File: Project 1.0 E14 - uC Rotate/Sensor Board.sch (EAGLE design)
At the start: 107 parts, among them IC1 LT1963EST-1.5, IC2 LT1963EST-1.5, IC4 LT1963EST-1.5, J1 501568-0207, J2 501568-0207, J3 SD-105027-101, U1 MAG3110, U10 ADXL362, U11 TM4C1233H6PM, U14 TXB0108, U15 ADT7301, U17 LSM9DS0, U19 MAX21000, U2 H3LIS331DLTR, U21 SN74HC42, U22 SI7013, U3 L3GD20H, U4 LPS331AP, U5 MPL3115A2, U6 LSM303D, U7 501568-0407, U8 STLM20, U9 LIS3DH

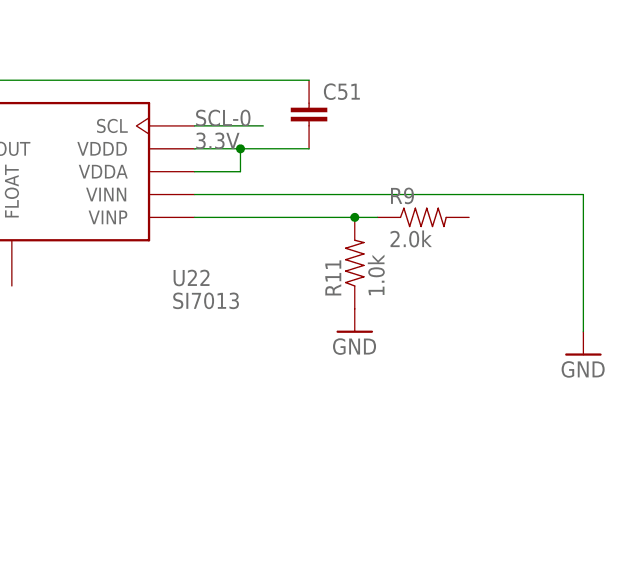
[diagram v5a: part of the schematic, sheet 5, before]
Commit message: Sensor Test Board: Resolved issue 22 by changing from LSG3 INT1 to INT2 allowing for an interupt to be genarated on a watermark event
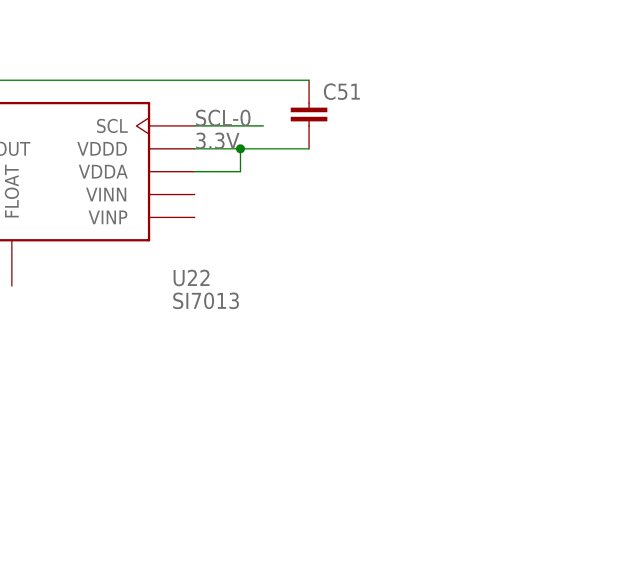
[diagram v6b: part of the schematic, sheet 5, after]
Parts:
- removed R11: 1.0k, Kas-Passives:RESISTOR
- removed R9: 2.0k, Kas-Passives:RESISTOR
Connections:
- removed net INT1-L3GD: U11.PC5, U3.INT1
- removed net N$2: R11.2, R9.1, U22.VINP
- new net INT2-L3GD: U11.PC5, U3.INT2
- net GND: no longer R11.1, U22.VINN
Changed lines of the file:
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@@
 <part name="R8" library="Kas-Passives" deviceset="RESISTOR" device="" value="0"/>
 <part name="U22" library="Kas-Sensors" deviceset="SI7013" device=""/>
-<part name="R9" library="Kas-Passives" deviceset="RESISTOR" device="" value="2.0k"/>
-<part name="R11" library="Kas-Passives" deviceset="RESISTOR" device="" value="1.0k"/>
 <part name="GND21" library="SparkFun-Aesthetics" deviceset="GND" device=""/>
 <part name="C51" library="Kas-Passives" deviceset="CAPACITOR" device="0402"/>
@@
 <part name="R14" library="Kas-Passives" deviceset="RESISTOR" device="" value="10k"/>
 <part name="GND22" library="SparkFun-Aesthetics" deviceset="GND" device=""/>
-<part name="GND39" library="SparkFun-Aesthetics" deviceset="GND" device=""/>
 <part name="GND40" library="SparkFun-Aesthetics" deviceset="GND" device=""/>
 <part name="GND41" library="SparkFun-Aesthetics" deviceset="GND" device=""/>
 <part name="GND45" library="SparkFun-Aesthetics" deviceset="GND" device=""/>
 <part name="GND46" library="SparkFun-Aesthetics" deviceset="GND" device=""/>
-<part name="GND49" library="SparkFun-Aesthetics" deviceset="GND" device=""/>
 <part name="J2" library="Kas-Connectors" deviceset="501568-0207" device=""/>
 <part name="LED5" library="eagle-ltspice" deviceset="LED_E" device="SML0603" value="Green"/>
@@
 <part name="GND50" library="SparkFun-Aesthetics" deviceset="GND" device=""/>
 <part name="GND51" library="SparkFun-Aesthetics" deviceset="GND" device=""/>
+<part name="GND52" library="SparkFun-Aesthetics" deviceset="GND" device=""/>
 </parts>
 <sheets>
@@
 </segment>
 </net>
-<net name="INT1-L3GD" class="0">
+<net name="INT2-L3GD" class="0">
 <segment>
 <pinref part="U11" gate="G$1" pin="PC5"/>
@@
 </segment>
 </net>
-<net name="INT1-L3GD" class="0">
-<segment>
-<pinref part="U3" gate="G$1" pin="INT1"/>
-<wire x1="43.18" y1="5.08" x2="43.18" y2="2.54" width="0.1524" layer="91"/>
+<net name="INT2-L3GD" class="0">
+<segment>
 <label x="25.4" y="2.54" size="1.778" layer="95"/>
-<wire x1="43.18" y1="2.54" x2="25.4" y2="2.54" width="0.1524" layer="91"/>
+<pinref part="U3" gate="G$1" pin="INT2"/>
+<wire x1="40.64" y1="2.54" x2="25.4" y2="2.54" width="0.1524" layer="91"/>
+<wire x1="40.64" y1="5.08" x2="40.64" y2="2.54" width="0.1524" layer="91"/>
 </segment>
 </net>
@@
 <instance part="GND44" gate="1" x="50.8" y="-17.78"/>
 <instance part="U22" gate="G$1" x="101.6" y="-7.62"/>
-<instance part="R9" gate="G$1" x="144.78" y="-12.7"/>
-<instance part="R11" gate="G$1" x="137.16" y="-17.78" rot="R90"/>
 <instance part="GND21" gate="1" x="73.66" y="-12.7"/>
 <instance part="C51" gate="G$1" x="132.08" y="-2.54"/>
-<instance part="GND39" gate="1" x="137.16" y="-25.4"/>
-<instance part="GND49" gate="1" x="162.56" y="-27.94"/>
 </instances>
 <busses>
@@
 <junction x="73.66" y="-10.16"/>
 <pinref part="C51" gate="G$1" pin="1"/>
-</segment>
-<segment>
-<pinref part="U22" gate="G$1" pin="VINN"/>
-<pinref part="GND49" gate="1" pin="GND"/>
-<wire x1="119.38" y1="-10.16" x2="162.56" y2="-10.16" width="0.1524" layer="91"/>
-<wire x1="162.56" y1="-10.16" x2="162.56" y2="-25.4" width="0.1524" layer="91"/>
-</segment>
-<segment>
-<pinref part="R11" gate="G$1" pin="1"/>
-<pinref part="GND39" gate="1" pin="GND"/>
 </segment>
 <segment>
@@
 </segment>
 </net>
-<net name="N$2" class="0">
-<segment>
-<pinref part="R9" gate="G$1" pin="1"/>
-<pinref part="R11" gate="G$1" pin="2"/>
-<wire x1="139.7" y1="-12.7" x2="137.16" y2="-12.7" width="0.1524" layer="91"/>
-<pinref part="U22" gate="G$1" pin="VINP"/>
-<wire x1="137.16" y1="-12.7" x2="119.38" y2="-12.7" width="0.1524" layer="91"/>
-<junction x="137.16" y="-12.7"/>
-</segment>
-</net>
 </nets>
 </sheet>
@@
 <instance part="GND50" gate="1" x="-25.4" y="2.54"/>
 <instance part="GND51" gate="1" x="27.94" y="2.54"/>
+<instance part="GND52" gate="1" x="30.48" y="-15.24"/>
 </instances>
 <busses>
@@
 <pinref part="U14" gate="G$1" pin="GND"/>
 <wire x1="15.24" y1="-12.7" x2="30.48" y2="-12.7" width="0.1524" layer="91"/>
-<label x="22.86" y="-12.7" size="1.778" layer="95"/>
-</segment>
-<segment>
+<pinref part="GND52" gate="1" pin="GND"/>
+</segment>
+<segment>

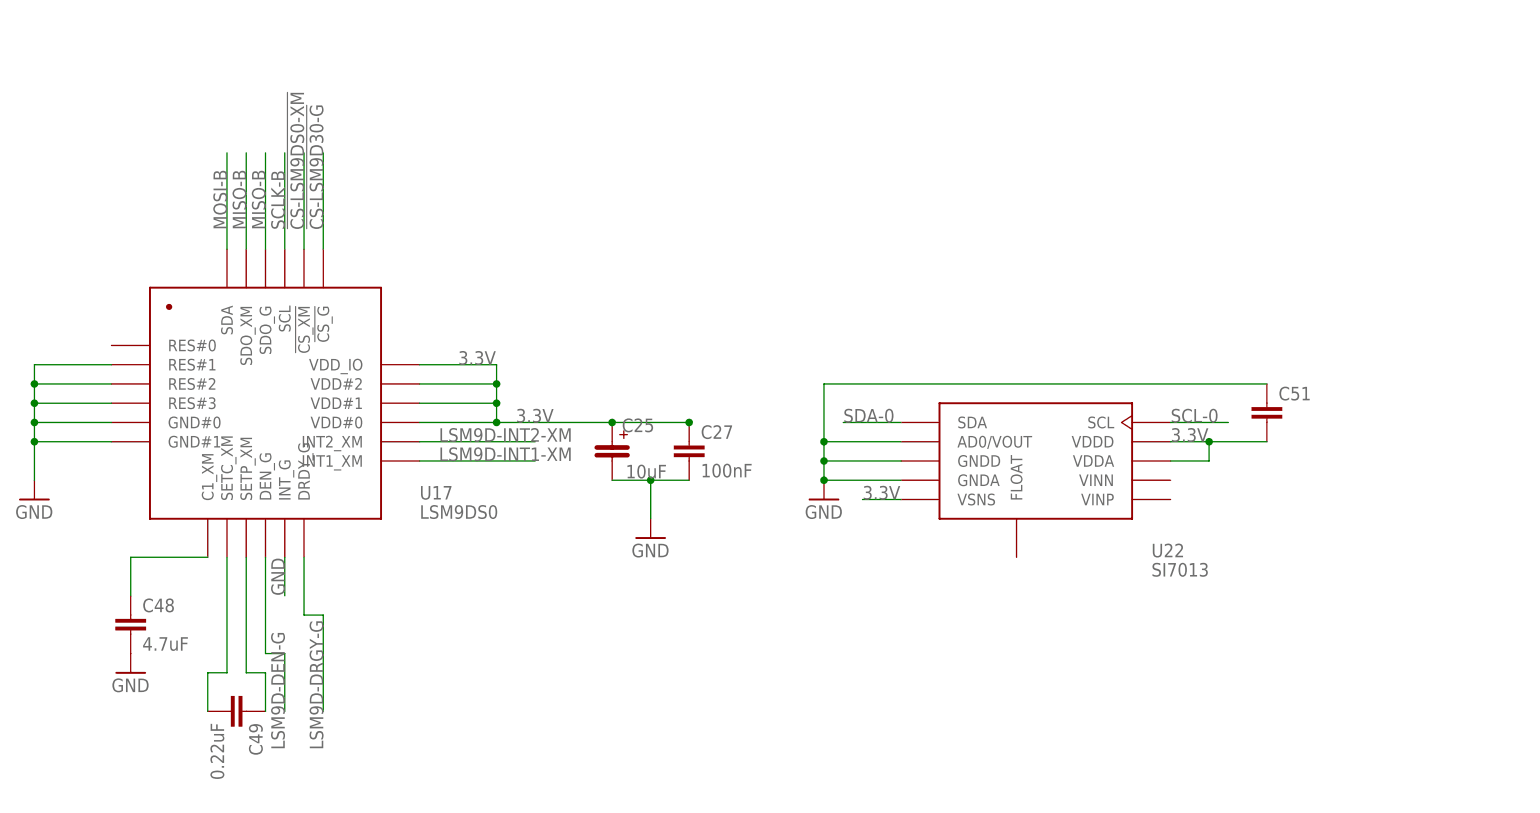
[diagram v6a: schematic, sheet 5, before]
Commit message: Sensor Test Board: Added power lines for all components. Split power into two groups A (130 mA) and B (177 mA). A has sensors connected except for the STLM20. B has the remaing components.  I2C test points were moved to allow for power routing to the right side sensors. Intterupt lines for ADXL362 and MPL3115A2 where swapped to allow for easier power routing
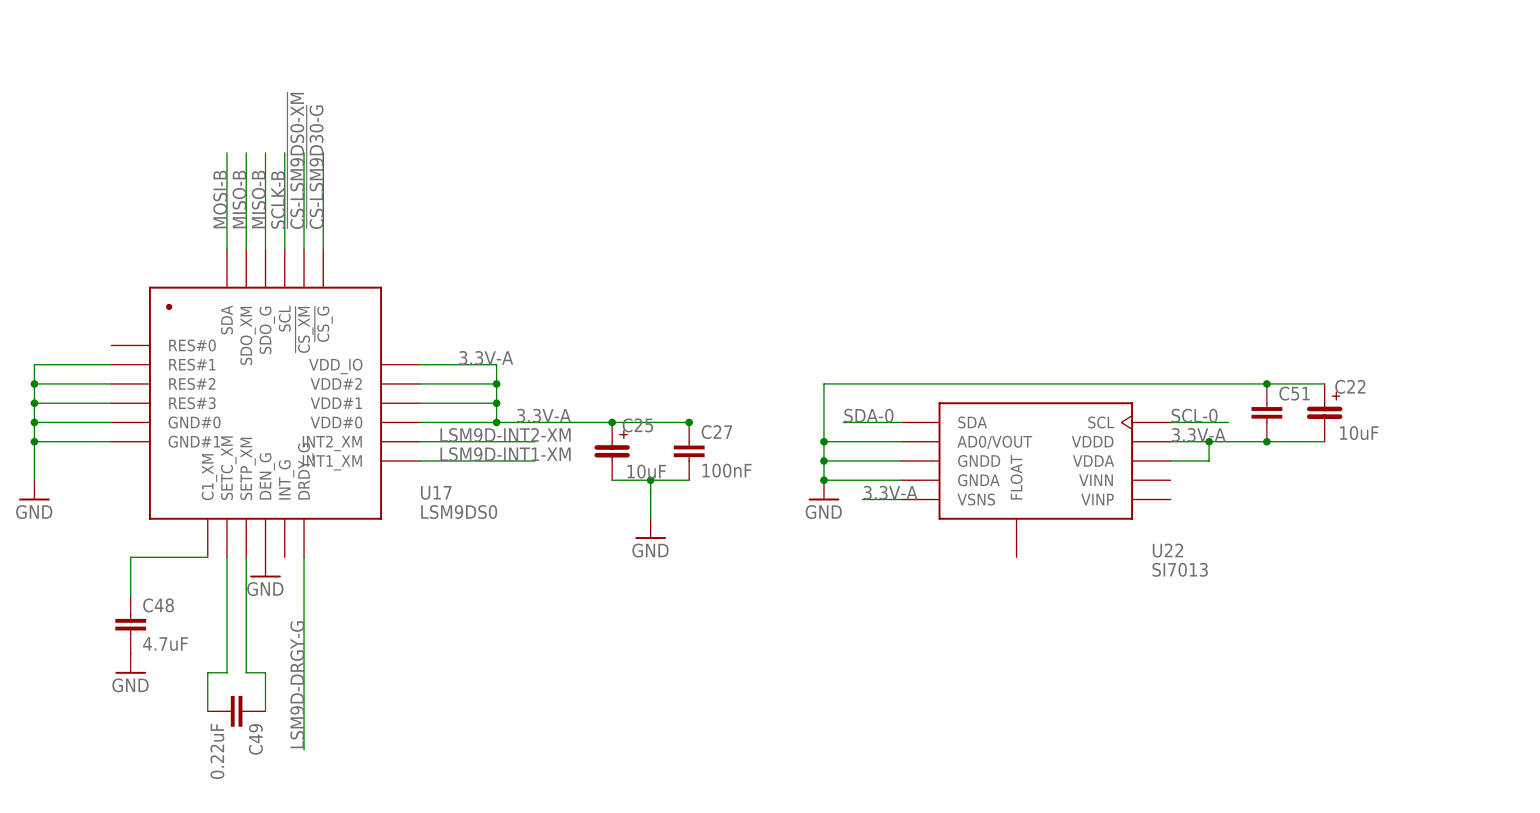
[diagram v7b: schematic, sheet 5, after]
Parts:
- added C22: 10uF, Kas-Passives:EEFCD0J100ER
- renumbered U$12 to X1, U$13 to X2, U7 to J4
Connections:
- removed net 3.3V: C11.1, C12.2, C13.@P$1, C14.2, C15.1, C16.1, C19.+, C2.1, C20.2, C23.1, C25.@P$1, C26.2, C27.1, C28.1, C29.2, C3.1, C35.2, C36.2, C37.2, C38.2, C39.2, C40.2, C45.@P$1, C46.@P$1, C47.@P$1, C5.1, C51.2, C52.1, C54.@P$1, C6.1, C7.@P$1, C8.1, C9.1, IC2G$1.OUT, J3.VDD, R1.2, R17.2, R2.2, R7.2, U1.VDD, U1.VDDIO, U10.VDD/IO, U10.VS, U11.VBAT, U11.VDD$0, U11.VDD$1, U11.VDD$2, U11.VDD$3, U11.VDDA, U14.VCCA, U14.VCCB, U15.VDD, U17.VDD#0, U17.VDD#1, U17.VDD#2, U17.VDD_IO, U19.VDD#0, U19.VDD#1, U19.VDDIO, U2.RSVD#1, U2.VDD, U2.VDDIO, U21.VCC, U22.VDDA, U22.VDDD, U22.VSNS, U3.RSVD$3, U3.VDD, U3.VDDIO, U4.VCCA, U4.VDD, U4.VDDIO, U5.VDD, U5.VDDIO, U6.VDD, U6.VDDIO, U8.VCC, U9.VDD, U9.VDD_IO
- removed net LSM9D-DEN-G: U17.DEN_G
- removed net N$23: IC1G$1.IN, IC2G$1.IN, IC4G$1.IN, S1.O
- new net 3.3V-A: C11.1, C12.2, C13.@P$1, C14.2, C15.1, C16.1, C19.+, C2.1, C20.2, C22.@P$2, C25.@P$1, C26.2, C27.1, C28.1, C29.2, C3.1, C45.@P$1, C46.@P$1, C47.@P$1, C5.1, C51.2, C52.1, C54.@P$1, C6.1, C7.@P$1, C8.1, C9.1, IC2G$1.OUT, U1.VDD, U1.VDDIO, U10.VDD/IO, U10.VS, U15.VDD, U17.VDD#0, U17.VDD#1, U17.VDD#2, U17.VDD_IO, U19.VDD#0, U19.VDD#1, U19.VDDIO, U2.RSVD#1, U2.VDD, U2.VDDIO, U22.VDDA, U22.VDDD, U22.VSNS, U3.RSVD$3, U3.VDD, U3.VDDIO, U4.VCCA, U4.VDD, U4.VDDIO, U5.VDD, U5.VDDIO, U6.VDD, U6.VDDIO, U9.VDD, U9.VDD_IO
- new net 3.3V-B: C23.1, C35.2, C36.2, C37.2, C38.2, C39.2, C40.2, IC1G$1.OUT, J3.VDD, R1.2, R17.2, R2.2, U11.VBAT, U11.VDD$0, U11.VDD$1, U11.VDD$2, U11.VDD$3, U11.VDDA, U14.VCCA, U14.VCCB, U21.VCC, U8.VCC
- new net POWER-IN: IC1G$1.IN, IC2G$1.IN, IC4G$1.IN, R7.2, S1.O
- net GND: now also C22.@P$1, J1.2, U17.DEN_G; no longer J1.1, U17.INT_G
- net INT1-MPL311: now also U11.PB7; no longer U11.PF4
- net INT2-ADXL362: now also U11.PF4; no longer U11.PB7
- net N$19: now also J1.1; no longer J1.2
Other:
- moved on the sheet: J1
